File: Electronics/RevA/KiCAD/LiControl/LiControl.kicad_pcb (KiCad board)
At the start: 2 copper layers, 1 part

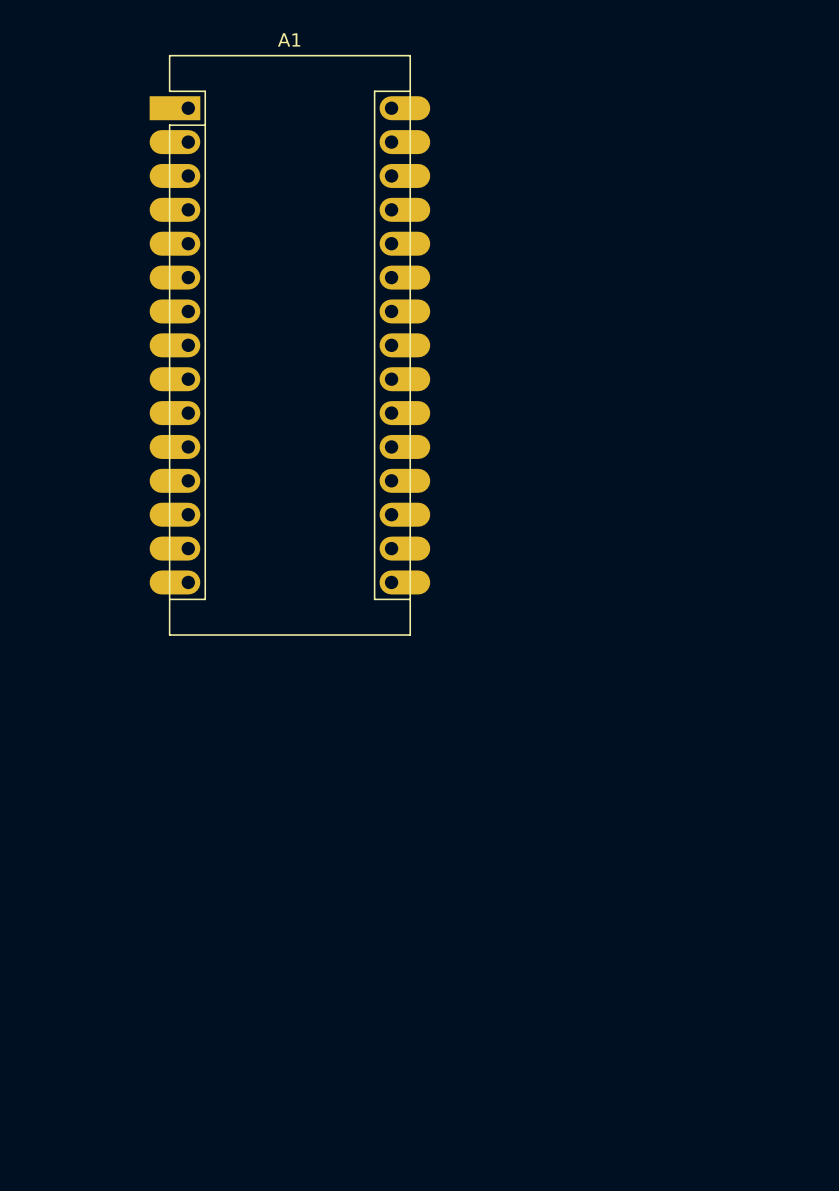
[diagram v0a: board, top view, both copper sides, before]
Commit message: RevA Schematic Finished, Starting Layout
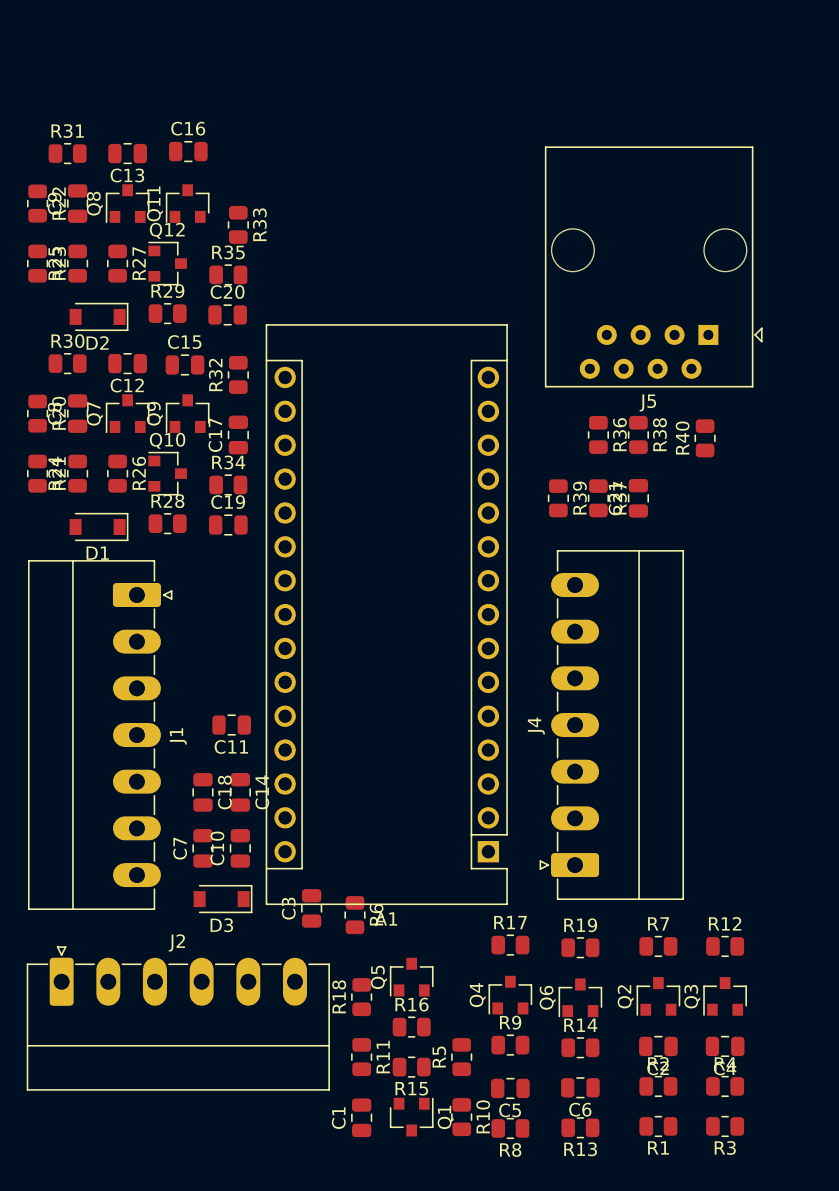
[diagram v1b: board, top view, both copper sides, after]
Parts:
- added C1: 100n, Capacitor_SMD:C_0805_2012Metric, F.Cu at (108.5, 118.2)
- added C10: 1u, Capacitor_SMD:C_0805_2012Metric, F.Cu at (99.4, 98.0)
- added C11: DNP, Capacitor_SMD:C_0805_2012Metric, F.Cu at (98.8, 88.8)
- added C12: 100n, Capacitor_SMD:C_0805_2012Metric, F.Cu at (91.0, 61.6)
- added C13: 100n, Capacitor_SMD:C_0805_2012Metric, F.Cu at (91.0, 45.9)
- added C14: 1u, Capacitor_SMD:C_0805_2012Metric, F.Cu at (99.4, 93.8)
- added C15: 1u, Capacitor_SMD:C_0805_2012Metric, F.Cu at (95.2, 61.8)
- added C16: 100n, Capacitor_SMD:C_0805_2012Metric, F.Cu at (95.5, 45.8)
- added C17: 100n, Capacitor_SMD:C_0805_2012Metric, F.Cu at (99.2, 67.0)
- added C18: 100n, Capacitor_SMD:C_0805_2012Metric, F.Cu at (96.6, 93.8)
- added C19: 1u, Capacitor_SMD:C_0805_2012Metric, F.Cu at (98.5, 73.8)
- added C2: 100n, Capacitor_SMD:C_0805_2012Metric, F.Cu at (130.8, 112.8)
- added C20: 100n, Capacitor_SMD:C_0805_2012Metric, F.Cu at (98.5, 58.0)
- added C21: 100n, Capacitor_SMD:C_0805_2012Metric, F.Cu at (129.2, 71.8)
- added C3: 100n, Capacitor_SMD:C_0805_2012Metric, F.Cu at (104.8, 102.5)
- added C4: 100n, Capacitor_SMD:C_0805_2012Metric, F.Cu at (135.8, 112.8)
- added C5: 100n, Capacitor_SMD:C_0805_2012Metric, F.Cu at (119.7, 116.0)
- added C6: 100n, Capacitor_SMD:C_0805_2012Metric, F.Cu at (124.9, 116.0)
- added C7: 100n, Capacitor_SMD:C_0805_2012Metric, F.Cu at (96.6, 98.0)
- added C8: 100p, Capacitor_SMD:C_0805_2012Metric, F.Cu at (87.2, 65.4)
- added C9: 100p, Capacitor_SMD:C_0805_2012Metric, F.Cu at (87.2, 49.6)
- added D1: D, Diode_SMD:D_SOD-123, F.Cu at (88.7, 73.9)
- added D2: D, Diode_SMD:D_SOD-123, F.Cu at (88.7, 58.1)
- added D3: D, Diode_SMD:D_SOD-123, F.Cu at (98.0, 101.8)
- added J1: Conn_01x07, Connector_Phoenix_MC:PhoenixContact_MC_1,5_7-G-3.5_1x07_P3.50mm_Horizontal, F.Cu at (91.7, 79.0)
- added J2: Conn_01x06, Connector_Phoenix_MC:PhoenixContact_MC_1,5_6-G-3.5_1x06_P3.50mm_Horizontal, F.Cu at (86.0, 108.0)
- added J4: Conn_01x07, Connector_Phoenix_MC:PhoenixContact_MC_1,5_7-G-3.5_1x07_P3.50mm_Horizontal, F.Cu at (124.5, 99.2)
- added J5: RJ45, Connector_RJ:RJ45_Amphenol_54602-x08_Horizontal, F.Cu at (134.5, 59.5)
- added Q1: Q_NMOS_GSD, Package_TO_SOT_SMD:SOT-23, F.Cu at (112.2, 118.2)
- added Q10: Q_NMOS_GSD, Package_TO_SOT_SMD:SOT-23, F.Cu at (94.0, 69.9)
- added Q11: Q_PMOS_GSD, Package_TO_SOT_SMD:SOT-23, F.Cu at (95.5, 49.6)
- added Q12: Q_NMOS_GSD, Package_TO_SOT_SMD:SOT-23, F.Cu at (94.0, 54.1)
- added Q2: Q_NMOS_GSD, Package_TO_SOT_SMD:SOT-23, F.Cu at (130.8, 109.1)
- added Q3: Q_NMOS_GSD, Package_TO_SOT_SMD:SOT-23, F.Cu at (135.8, 109.1)
- added Q4: Q_NMOS_GSD, Package_TO_SOT_SMD:SOT-23, F.Cu at (119.7, 109.0)
- added Q5: Q_NMOS_GSD, Package_TO_SOT_SMD:SOT-23, F.Cu at (112.2, 107.7)
- added Q6: Q_NMOS_GSD, Package_TO_SOT_SMD:SOT-23, F.Cu at (124.9, 109.2)
- added Q7: Q_PMOS_GSD, Package_TO_SOT_SMD:SOT-23, F.Cu at (91.0, 65.4)
- added Q8: Q_PMOS_GSD, Package_TO_SOT_SMD:SOT-23, F.Cu at (91.0, 49.6)
- added Q9: Q_PMOS_GSD, Package_TO_SOT_SMD:SOT-23, F.Cu at (95.5, 65.4)
- added R1: 1k24, Resistor_SMD:R_0805_2012Metric, F.Cu at (130.8, 118.8)
- added R10: DNP, Resistor_SMD:R_0805_2012Metric, F.Cu at (116.0, 118.2)
- added R11: DNP, Resistor_SMD:R_0805_2012Metric, F.Cu at (108.5, 113.7)
- added R12: 1k24, Resistor_SMD:R_0805_2012Metric, F.Cu at (135.8, 105.3)
- added R13: 1k24, Resistor_SMD:R_0805_2012Metric, F.Cu at (124.9, 119.0)
- added R14: DNP, Resistor_SMD:R_0805_2012Metric, F.Cu at (124.9, 113.0)
- added R15: DNP, Resistor_SMD:R_0805_2012Metric, F.Cu at (112.2, 114.4)
- added R16: DNP, Resistor_SMD:R_0805_2012Metric, F.Cu at (112.2, 111.4)
- added R17: 1k24, Resistor_SMD:R_0805_2012Metric, F.Cu at (119.7, 105.2)
- added R18: DNP, Resistor_SMD:R_0805_2012Metric, F.Cu at (108.5, 109.2)
- added R19: 1k24, Resistor_SMD:R_0805_2012Metric, F.Cu at (124.9, 105.5)
- added R2: DNP, Resistor_SMD:R_0805_2012Metric, F.Cu at (130.8, 115.8)
- added R20: 1k24, Resistor_SMD:R_0805_2012Metric, F.Cu at (84.2, 65.4)
- added R21: 768, Resistor_SMD:R_0805_2012Metric, F.Cu at (84.2, 69.9)
- added R22: 1k24, Resistor_SMD:R_0805_2012Metric, F.Cu at (84.2, 49.6)
- added R23: 768, Resistor_SMD:R_0805_2012Metric, F.Cu at (84.2, 54.1)
- added R24: 1k24, Resistor_SMD:R_0805_2012Metric, F.Cu at (87.2, 69.9)
- added R25: 1k24, Resistor_SMD:R_0805_2012Metric, F.Cu at (87.2, 54.1)
- added R26: 1k24, Resistor_SMD:R_0805_2012Metric, F.Cu at (90.2, 69.9)
- added R27: 1k24, Resistor_SMD:R_0805_2012Metric, F.Cu at (90.2, 54.1)
- added R28: DNP, Resistor_SMD:R_0805_2012Metric, F.Cu at (94.0, 73.7)
- added R29: DNP, Resistor_SMD:R_0805_2012Metric, F.Cu at (94.0, 57.9)
- added R3: 1k24, Resistor_SMD:R_0805_2012Metric, F.Cu at (135.8, 118.8)
- added R30: 20, Resistor_SMD:R_0805_2012Metric, F.Cu at (86.5, 61.6)
- added R31: 20, Resistor_SMD:R_0805_2012Metric, F.Cu at (86.5, 45.9)
- added R32: 1k24, Resistor_SMD:R_0805_2012Metric, F.Cu at (99.2, 62.5)
- added R33: 1k24, Resistor_SMD:R_0805_2012Metric, F.Cu at (99.2, 51.2)
- added R34: 7k32, Resistor_SMD:R_0805_2012Metric, F.Cu at (98.5, 70.8)
- added R35: 7k32, Resistor_SMD:R_0805_2012Metric, F.Cu at (98.5, 55.0)
- added R36: 10k, Resistor_SMD:R_0805_2012Metric, F.Cu at (126.2, 67.0)
- added R37: 10k, Resistor_SMD:R_0805_2012Metric, F.Cu at (126.2, 71.8)
- added R38: 10k, Resistor_SMD:R_0805_2012Metric, F.Cu at (129.2, 67.0)
- added R39: 10k, Resistor_SMD:R_0805_2012Metric, F.Cu at (123.2, 71.8)
- added R4: 1k24, Resistor_SMD:R_0805_2012Metric, F.Cu at (135.8, 115.8)
- added R40: 10k, Resistor_SMD:R_0805_2012Metric, F.Cu at (134.2, 67.2)
- added R5: DNP, Resistor_SMD:R_0805_2012Metric, F.Cu at (116.0, 113.7)
- added R6: 1k24, Resistor_SMD:R_0805_2012Metric, F.Cu at (108.0, 103.0)
- added R7: 1k24, Resistor_SMD:R_0805_2012Metric, F.Cu at (130.8, 105.3)
- added R8: 7k32, Resistor_SMD:R_0805_2012Metric, F.Cu at (119.7, 119.0)
- added R9: 7k32, Resistor_SMD:R_0805_2012Metric, F.Cu at (119.7, 112.8)
- A1: value Arduino_Nano_Every -> Arduino_Nano_v3.x; footprint Module:Arduino_Nano_Castellated -> Module:Arduino_Nano
- moved A1 60.1 mm to (118.0, 98.2), turned to 180 degrees
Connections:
- net Net-(A1-Pad29) renamed GND
- A1 pad 10: (no net) -> /VSS_PCINT2
- A1 pad 11: (no net) -> /NEP_PCINT0
- A1 pad 12: (no net) -> /CMDPWR_MCM
- A1 pad 18: (no net) -> /AREF
- A1 pad 19: (no net) -> /POTENTIOMETER
- A1 pad 20: (no net) -> /MAMODE1_ADC
- A1 pad 21: (no net) -> /CMDPWR_ADC
- A1 pad 22: (no net) -> /BUTTON
- A1 pad 23: (no net) -> /MODE_SEL1
- A1 pad 24: (no net) -> /MODE_SEL2
- A1 pad 25: (no net) -> /GPIO
- A1 pad 26: (no net) -> /THROTTLE
- A1 pad 27: (no net) -> +5V
- A1 pad 28: (no net) -> /RESETn
- A1 pad 30: (no net) -> /12V_VIN
- A1 pad 5: (no net) -> /MAMODE2_MCM
- A1 pad 6: (no net) -> /MAMODE1_MCM
- A1 pad 7: (no net) -> /MAMODE2_ECM
- A1 pad 8: (no net) -> /BRAKE_BUFF
- A1 pad 9: (no net) -> /CLUTCH_BUFF
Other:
- board text added: "ECM"
- board text added: "MCM"
- board text added: "ROUGH FOOTPRINT"
- board text added: "USB (ROUGH)"

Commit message: Final RevA PCB
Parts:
- added J3: Conn_01x03, Connector_Phoenix_MC:PhoenixContact_MCV_1,5_3-G-3.5_1x03_P3.50mm_Vertical, F.Cu at (127.2, 111.0)
- added REF**: OSHW-Logo2_7.3x6mm_SilkScreen, Symbol:OSHW-Logo2_7.3x6mm_SilkScreen, F.Cu at (98.2, 105.2)
- C1, C10, C11, C12, C13, C14, C15, C16, C17, C18, C19, C2, C20, C21, C3, C4, C5, C6, C7, C8, C9, D1, D2, D3, Q1, Q10, Q11, Q12, Q2, Q3, Q4, Q5, Q6, Q7, Q8, Q9, R1, R10, R11, R12, R13, R14, R15, R16, R17, R18, R19, R2, R20, R21, R22, R23, R24, R25, R26, R27, R28, R29, R3, R30, R31, R32, R33, R34, R35, R36, R37, R38, R39, R4, R40, R5, R6, R7, R8, R9: moved to B.Cu
- J1, J4: footprint Connector_Phoenix_MC:PhoenixContact_MC_1,5_7-G-3.5_1x07_P3.50mm_Horizontal -> Connector_Phoenix_MC:PhoenixContact_MCV_1,5_7-G-3.5_1x07_P3.50mm_Vertical
- J2: value Conn_01x06 -> Conn_01x03; footprint Connector_Phoenix_MC:PhoenixContact_MC_1,5_6-G-3.5_1x06_P3.50mm_Horizontal -> Connector_Phoenix_MC:PhoenixContact_MCV_1,5_3-G-3.5_1x03_P3.50mm_Vertical
- moved R8 56.2 mm to (94.0, 69.0), turned to 270 degrees
- moved J2 49.2 mm to (96.8, 60.0), turned to 180 degrees
- moved C5 49.2 mm to (96.8, 72.5)
- moved R30 44.8 mm to (114.8, 96.2), turned to 90 degrees
- moved R9 44.0 mm to (96.7, 75.2)
- moved R20 42.6 mm to (111.2, 98.2), turned to 180 degrees
- moved R22 40.4 mm to (114.0, 77.0), turned to 180 degrees
- moved R6 39.8 mm to (97.8, 64.5), turned to 180 degrees
- moved R31 38.8 mm to (114.5, 72.8), turned to 90 degrees
- moved C8 38.7 mm to (111.2, 95.8), turned to 0 degrees
- moved C12 38.0 mm to (114.8, 91.2), turned to 270 degrees
- moved Q4 37.8 mm to (96.7, 79.0), turned to 270 degrees
- moved R21 35.4 mm to (107.0, 97.0), turned to 180 degrees
- moved R23 34.3 mm to (109.8, 77.0), turned to 180 degrees
- moved C9 33.0 mm to (110.8, 72.8)
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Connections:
- J2 pad 1: GND -> /THROTTLE_RAW
- J2 pad 2: +5V -> /CLUTCH_RAW
- J2 pad 3: /GPIO_RAW -> /BRAKE_RAW
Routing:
- net GND: track 0.00 -> 391.0 mm, vias 0 -> 17
- net +5V: track 0.00 -> 188.9 mm, vias 0 -> 12
- net /12V_KEYON: track 0.00 -> 99.6 mm, vias 0 -> 3
- net /CLUTCH_RAW: track 0.00 -> 77.4 mm, vias 0 -> 5
- net /NEP_12V: track 0.00 -> 61.0 mm
- net /VSS: track 0.00 -> 60.3 mm, vias 0 -> 2
- net /GPIO: track 0.00 -> 50.0 mm, vias 0 -> 2
- net /CMDPWR_ECM: track 0.00 -> 48.6 mm, vias 0 -> 1
- net /POTENTIOMETER: track 0.00 -> 47.3 mm, vias 0 -> 1
- net /BUTTON: track 0.00 -> 41.1 mm, vias 0 -> 1
- net /MODE_SEL2: track 0.00 -> 40.0 mm
- net /MAMODE1_ECM: track 0.00 -> 36.6 mm, vias 0 -> 1
- net /MODE_SEL1: track 0.00 -> 34.0 mm
- net /MAMODE2_ECM: track 0.00 -> 33.4 mm, vias 0 -> 1
- net /MAMODE2_MCM: track 0.00 -> 33.4 mm, vias 0 -> 1
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- added copper zone on B.Cu, net +5V
- added copper zone on F.Cu, net +5V
- added copper zone on B.Cu, net /12V_VIN
- added copper zone on B.Cu, net /CMD_5V_ILIM
- added copper zone on B.Cu, net /CMD_G2
- added copper zone on B.Cu, net /MA1_5V_ILIM
- added copper zone on B.Cu, net /MA1_G2
- added copper zone on B.Cu, net GND
- added copper zone on F.Cu, net GND
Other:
- board outline added: 56 x 59 mm
- board text added: "??? 5V GND"
- board text added: "BLK/YEL RED/YEL BLU/BLK BRN/YEL PNK/BLU BLU/BLU BLU/WHT"
- board text added: "BRAKE CLUTCH TPS"
- board text added: "GND POT 5V GND BUTTON MODE1 MODE2 GND"
- board text added: "HMI"
- board text added: "LiControl"
- board text added: "MA2 MA1 CMD GND 12V NEP VSS"
- board text added: "RevA"
- board text added: "github.com/ doppelhub/ MuddersMIMA"
- board text removed: "ROUGH FOOTPRINT"
